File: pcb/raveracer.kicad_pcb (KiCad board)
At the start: 2 copper layers, 125.1 x 44 mm, 14 parts, among them J1 System22_Video_PCB, J2 SCART-F, J3 DEBUG, J4 VGA-F, U1 LM1881

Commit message: continue routing
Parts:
- added J5: Power Supply, TerminalBlock_Phoenix:TerminalBlock_Phoenix_MKDS-1,5-2-5.08_1x02_P5.08mm_Horizontal, F.Cu at (120.0, 70.7)
- moved R1 3.09 mm to (98.8, 72.0)
- moved R2 3.04 mm to (106.5, 77.2)
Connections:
- J4 pad 13: /CSYNC -> Net-(J4-Pad13)
- J4 pad 14: (no net) -> Net-(J4-Pad14)
- U1 pad 1: (no net) -> Net-(J4-Pad13)
- U1 pad 3: (no net) -> Net-(J4-Pad14)
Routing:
- net Net-(J4-Pad14): track 0.00 -> 33.1 mm, vias 0 -> 2
- net Net-(J4-Pad13): track 0.00 -> 27.1 mm, vias 0 -> 1
- net +12V: track 71.4 -> 92.1 mm
- net GND: track 299.5 -> 313.0 mm, vias 5 -> 6
- net Net-(J2-Pad16): track 40.5 -> 46.7 mm
- net /CSYNC: track 126.2 -> 124.6 mm, vias 4 -> 5
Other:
- board text added: "+12V"

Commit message: finished routing of pcb
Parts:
- moved J2 3.72 mm to (82.3, 56.5)
- moved J4 3.63 mm to (28.1, 66.7)
- moved H3 1.41 mm to (119.0, 85.0)
- moved H1 1.00 mm to (6.00, 85.0)
- moved H4 1.00 mm to (119.0, 52.0)
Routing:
- net /CSYNC: track 124.6 -> 135.0 mm, vias 5 -> 3
- net Net-(J4-Pad14): track 33.1 -> 42.6 mm, vias 2 -> 4
- net /Blue: track 84.8 -> 80.7 mm, vias 4 -> 3
- net /Green: track 83.3 -> 79.8 mm, vias 5 -> 3
- net Net-(J2-Pad16): track 46.7 -> 43.9 mm
- net /Red: track 92.3 -> 93.7 mm, vias 5 -> 4
- net Net-(J4-Pad13): track 27.1 -> 25.8 mm
- net GND: track 313.0 -> 312.1 mm, vias 6 -> 5
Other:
- board size 125.1 x 44 mm -> 125 x 45 mm
- board text added: "System 22 Video In"
- board text added: "cascha coon 10/2020"
- board text removed: "cascha coon 09/2020"

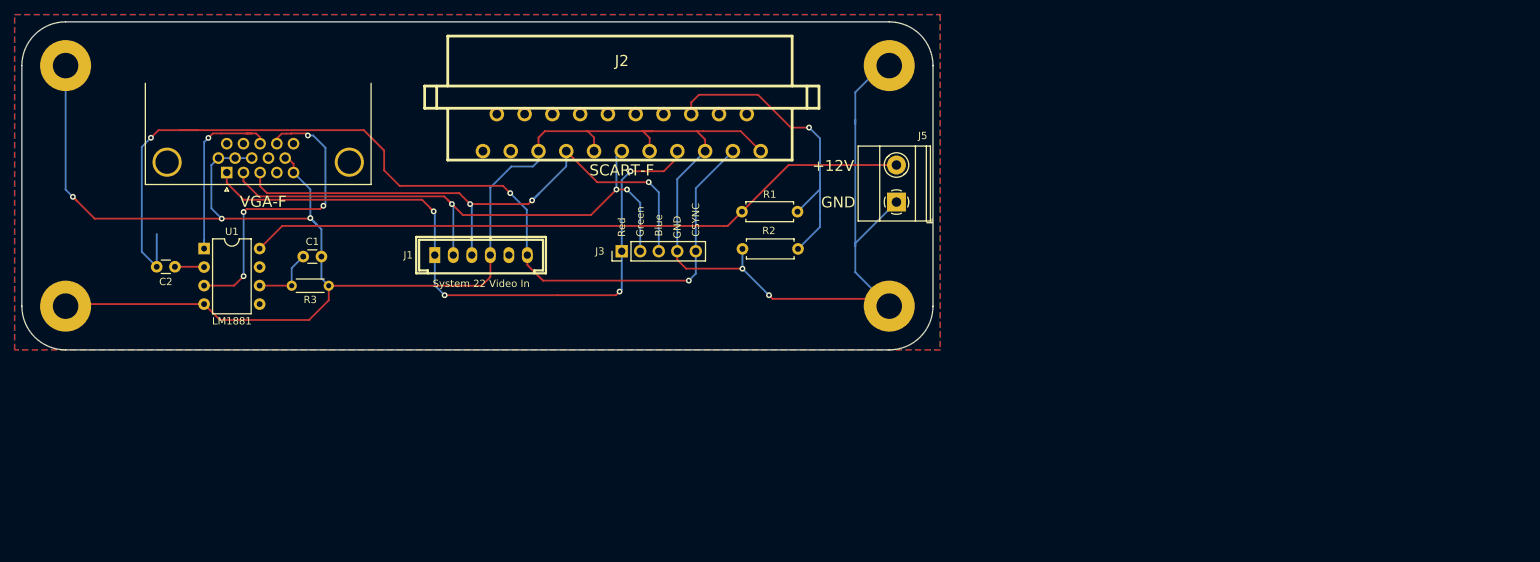
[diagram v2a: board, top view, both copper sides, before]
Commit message: fix routing of modified ampmodu connector
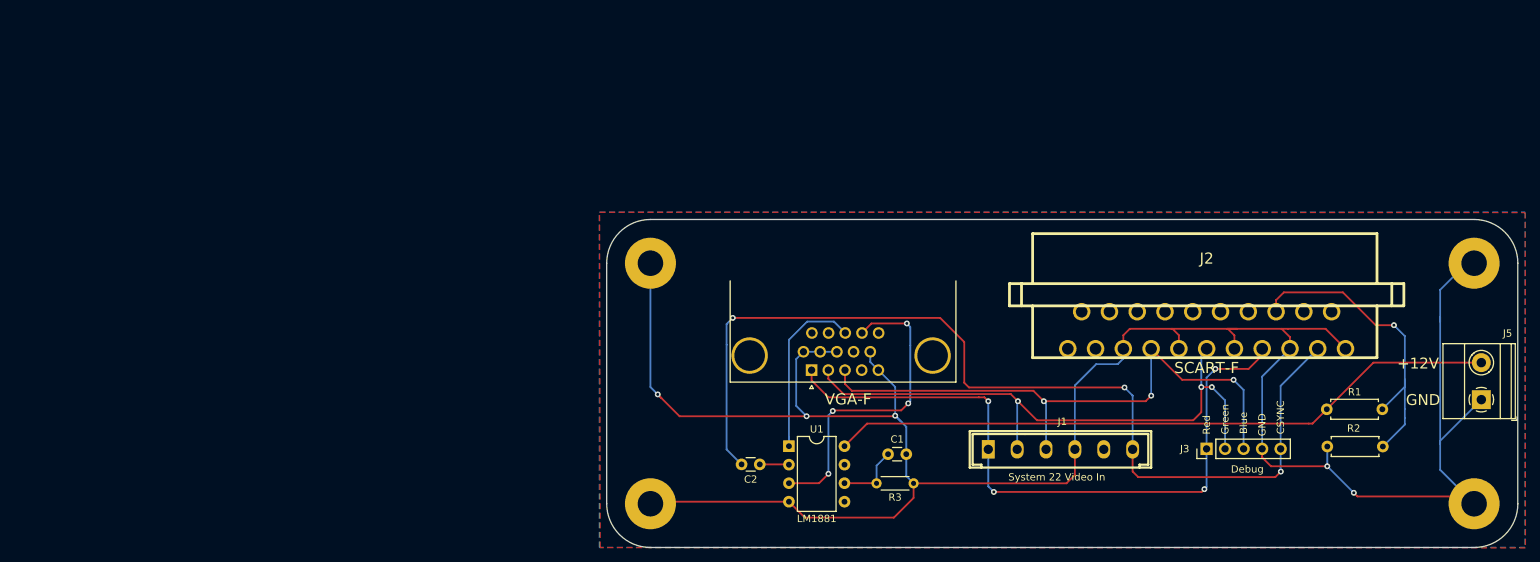
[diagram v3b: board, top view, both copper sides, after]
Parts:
- J1: footprint w_conn_modu:AMP-MODU-6 -> ampmodu-custom:AMP-MODU-6-3p96mm-mod
- J3: value DEBUG -> Debug
- moved C2 84.7 mm to (101.2, 106.7)
- moved H1 84.7 mm to (86.2, 112.1)
- moved H2 84.7 mm to (86.2, 79.1)
- moved J2 84.7 mm to (162.5, 83.6)
- moved J3 84.7 mm to (162.5, 104.6)
- moved J4 84.7 mm to (108.3, 93.8)
- moved J5 84.7 mm to (200.2, 97.8)
- moved R1 84.7 mm to (179.0, 99.2)
- moved R2 84.7 mm to (186.7, 104.3)
- moved U1 84.7 mm to (105.2, 104.2)
- moved C1 84.7 mm to (118.8, 105.3)
- moved H3 84.7 mm to (199.2, 112.1)
- moved H4 84.7 mm to (199.2, 79.1)
- moved R3 84.7 mm to (122.3, 109.3)
- moved J1 80.5 mm to (138.9, 104.6)
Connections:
- J1 pad 5: (no net) -> unconnected-(J1-Pad5)
- J2 pad 1: (no net) -> unconnected-(J2-Pad1)
- J2 pad 10: (no net) -> unconnected-(J2-Pad10)
- J2 pad 12: (no net) -> unconnected-(J2-Pad12)
- J2 pad 14: (no net) -> GND
- J2 pad 18: (no net) -> GND
- J2 pad 2: (no net) -> unconnected-(J2-Pad2)
- J2 pad 20: (no net) -> unconnected-(J2-Pad20)
- J2 pad 3: (no net) -> unconnected-(J2-Pad3)
- J2 pad 4: (no net) -> GND
- J2 pad 6: (no net) -> unconnected-(J2-Pad6)
- J2 pad 8: (no net) -> unconnected-(J2-Pad8)
- J4 pad 11: (no net) -> unconnected-(J4-Pad11)
- J4 pad 12: (no net) -> unconnected-(J4-Pad12)
- J4 pad 15: (no net) -> unconnected-(J4-Pad15)
- J4 pad 4: (no net) -> unconnected-(J4-Pad4)
- J4 pad 9: (no net) -> unconnected-(J4-Pad9)
- U1 pad 5: (no net) -> unconnected-(U1-Pad5)
- U1 pad 7: (no net) -> unconnected-(U1-Pad7)
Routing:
- net Net-(J4-Pad14): track 42.6 -> 44.5 mm
- net /Green: track 79.8 -> 81.5 mm
- net GND: track 312.1 -> 313.3 mm
- net /CSYNC: track 135.0 -> 134.1 mm
- net /Blue: track 80.7 -> 81.5 mm
- net Net-(J4-Pad13): track 25.8 -> 26.0 mm, vias 1 -> 0
- added copper zone on B.Cu, net GND
- added copper zone on F.Cu, net GND
- removed copper zone on B.Cu, net (none)
- removed copper zone on F.Cu, net (none)
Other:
- net class Default removed
- board text added: "cascha coon 04/2023"
- board text removed: "cascha coon 10/2020"
